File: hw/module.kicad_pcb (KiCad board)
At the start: 2 copper layers, 30 x 30 mm, 1 part

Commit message: Footprint assignment
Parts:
- added C1: 10n, Capacitor_SMD:C_0201_0603Metric_Pad0.64x0.40mm_HandSolder, F.Cu at (99.5, 62.5)
- added C10: 10n, Capacitor_SMD:C_0201_0603Metric_Pad0.64x0.40mm_HandSolder, F.Cu at (106.8, 52.8)
- added C11: 100n, Capacitor_SMD:C_0805_2012Metric_Pad1.18x1.45mm_HandSolder, F.Cu at (95.7, 63.1)
- added C12: 100n, Capacitor_SMD:C_0805_2012Metric_Pad1.18x1.45mm_HandSolder, F.Cu at (90.9, 65.9)
- added C13: 100n, Capacitor_SMD:C_0805_2012Metric_Pad1.18x1.45mm_HandSolder, F.Cu at (90.9, 62.9)
- added C14: 100n, Capacitor_SMD:C_0805_2012Metric_Pad1.18x1.45mm_HandSolder, F.Cu at (102.9, 53.4)
- added C2: 10n, Capacitor_SMD:C_0201_0603Metric_Pad0.64x0.40mm_HandSolder, F.Cu at (84.5, 67.4)
- added C3: 100n, Capacitor_SMD:C_0201_0603Metric_Pad0.64x0.40mm_HandSolder, F.Cu at (94.7, 65.5)
- added C4: 100n, Capacitor_SMD:C_0201_0603Metric_Pad0.64x0.40mm_HandSolder, F.Cu at (105.6, 58.0)
- added C5: 200p, Capacitor_SMD:C_0201_0603Metric_Pad0.64x0.40mm_HandSolder, F.Cu at (102.8, 57.6)
- added C6: 200p, Capacitor_SMD:C_0201_0603Metric_Pad0.64x0.40mm_HandSolder, F.Cu at (106.8, 54.5)
- added C7: 10n, Capacitor_SMD:C_0201_0603Metric_Pad0.64x0.40mm_HandSolder, F.Cu at (94.7, 67.3)
- added C8: 100n, Capacitor_SMD:C_0201_0603Metric_Pad0.64x0.40mm_HandSolder, F.Cu at (105.6, 56.3)
- added C9: 100n, Capacitor_SMD:C_0201_0603Metric_Pad0.64x0.40mm_HandSolder, F.Cu at (109.6, 52.8)
- added L1: L, Inductor_SMD:L_0201_0603Metric_Pad0.64x0.40mm_HandSolder, F.Cu at (108.4, 56.3)
- added R1: 10k, Resistor_SMD:R_0201_0603Metric_Pad0.64x0.40mm_HandSolder, F.Cu at (100.0, 59.2)
- added R2: 10k, Resistor_SMD:R_0201_0603Metric_Pad0.64x0.40mm_HandSolder, F.Cu at (97.5, 67.3)
- added R3: 800k, Resistor_SMD:R_0201_0603Metric_Pad0.64x0.40mm_HandSolder, F.Cu at (102.8, 55.8)
- added R4: 800k, Resistor_SMD:R_0201_0603Metric_Pad0.64x0.40mm_HandSolder, F.Cu at (97.5, 65.5)
- added R5: R, Resistor_SMD:R_0201_0603Metric_Pad0.64x0.40mm_HandSolder, F.Cu at (102.3, 61.1)
- added R6: 500k, Resistor_SMD:R_0201_0603Metric_Pad0.64x0.40mm_HandSolder, F.Cu at (109.6, 54.5)
- added R7: 500k, Resistor_SMD:R_0201_0603Metric_Pad0.64x0.40mm_HandSolder, F.Cu at (100.0, 57.5)
- added R8: 10k, Resistor_SMD:R_0201_0603Metric_Pad0.64x0.40mm_HandSolder, F.Cu at (102.8, 59.3)
- added TP1: SWDIO, TestPoint:TestPoint_Pad_3.0x3.0mm, F.Cu at (91.0, 58.9)
- added TP2: SWCLK, TestPoint:TestPoint_Pad_3.0x3.0mm, F.Cu at (96.0, 59.1)
- added U1: CFPS-39, Oscillator:Oscillator_SMD_Fox_FT5H_5.0x3.2mm, F.Cu at (85.8, 55.6)
- added U2: CFPS-39, Oscillator:Oscillator_SMD_Fox_FT5H_5.0x3.2mm, F.Cu at (85.8, 62.9)
- added U3: 74LVC1G125, Package_TO_SOT_SMD:SOT-23-5_HandSoldering, F.Cu at (124.5, 66.5)
- added U4: mux, Package_TO_SOT_SMD:SOT-363_SC-70-6_Handsoldering, F.Cu at (124.5, 62.2)
- added U5: MAX919, Package_TO_SOT_SMD:SOT-23-5_HandSoldering, F.Cu at (97.6, 54.2)
- added U6: STM32L010F4P6, farnell:STM32L010F4P6, F.Cu at (115.9, 68.4)
- added U7: BAS70-7-F, Package_TO_SOT_SMD:SOT-143_Handsoldering, F.Cu at (91.6, 54.1)

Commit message: PCB arrange
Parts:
- moved U4 76.0 mm to (49.0, 52.9), turned to -90 degrees
- moved U3 75.6 mm to (51.2, 48.0), turned to 90 degrees
- moved R6 64.2 mm to (45.4, 56.8)
- moved L1 62.5 mm to (46.6, 65.4), turned to 90 degrees
- moved U6 62.5 mm to (53.6, 63.5), turned to -90 degrees
- moved R5 56.9 mm to (46.0, 69.2)
- moved C1 56.8 mm to (44.4, 48.8), turned to -90 degrees
- moved C14 54.0 mm to (49.2, 58.2)
- moved C6 51.7 mm to (56.2, 43.6)
- moved R7 51.0 mm to (49.0, 56.8)
- moved R2 50.9 mm to (52.0, 44.4)
- moved R1 50.0 mm to (52.0, 45.2)
- moved C11 48.3 mm to (47.6, 67.6)
- moved R8 47.4 mm to (55.4, 57.8), turned to -90 degrees
- moved R4 47.1 mm to (56.2, 42.8)
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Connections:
- U7 pad 1: Net-(C6-Pad1) -> Net-(R1-Pad2)
- U7 pad 2: Net-(R1-Pad2) -> Net-(C6-Pad1)
- U7 pad 3: Net-(C5-Pad2) -> Net-(R2-Pad2)
- U7 pad 4: Net-(R2-Pad2) -> Net-(C5-Pad2)

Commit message: PCB wiring
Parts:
- moved C3 38.5 mm to (53.3, 50.8), turned to 180 degrees
- moved C7 36.8 mm to (53.3, 67.9), turned to 180 degrees
- moved C8 30.2 mm to (53.3, 69.2), turned to 180 degrees
- moved C9 25.2 mm to (61.6, 59.1), turned to 90 degrees
- moved C10 25.1 mm to (59.1, 62.2), turned to 90 degrees
- moved C4 23.1 mm to (60.3, 59.1), turned to 90 degrees
- moved C6 8.58 mm to (62.4, 49.5), turned to 90 degrees
- moved R4 6.94 mm to (61.2, 47.6)
- moved C2 6.83 mm to (57.8, 62.2), turned to 90 degrees
- moved U5 5.66 mm to (59.9, 51.4), turned to 90 degrees
- moved C5 4.22 mm to (55.9, 52.7)
- moved R7 4.19 mm to (49.5, 61.0), turned to 90 degrees
- moved R2 3.76 mm to (54.0, 47.6), turned to -90 degrees
- moved C13 3.74 mm to (47.0, 61.6)
- moved C1 3.53 mm to (45.7, 52.1)
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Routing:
- net +3.3V: track 0.00 -> 55.4 mm
- net /OSC_STAT: track 0.00 -> 19.5 mm
- net +3.3VA: track 0.00 -> 16.8 mm
- net /half_vref: track 0.00 -> 12.9 mm
- net Net-(C5-Pad2): track 0.00 -> 11.5 mm
- net Net-(C6-Pad1): track 0.00 -> 10.8 mm
- net /OSC: track 0.00 -> 9.85 mm
- net Net-(TP1-Pad1): track 0.00 -> 8.89 mm
- net Net-(U1-Pad3): track 0.00 -> 6.77 mm
- net Net-(TP2-Pad1): track 0.00 -> 6.22 mm
- net Net-(C11-Pad1): track 0.00 -> 5.46 mm
- net Net-(U2-Pad3): track 0.00 -> 5.24 mm
- net Net-(R1-Pad2): track 0.00 -> 4.85 mm
- net Net-(R8-Pad2): track 0.00 -> 3.58 mm
- net Net-(R1-Pad1): track 0.00 -> 3.29 mm
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- removed copper zone on B.Cu, net GND
- removed copper zone on F.Cu, net GND

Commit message: Pcb++
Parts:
- added C15: 1n, Capacitor_SMD:C_0201_0603Metric_Pad0.64x0.40mm_HandSolder, F.Cu at (54.6, 58.7)
- U4: value mux -> 74 LVC 1G3157GW,125
- moved C4 5.75 mm to (58.2, 64.4), turned to 0 degrees
- moved C9 5.67 mm to (58.2, 63.6), turned to 0 degrees
- moved C1 3.44 mm to (44.5, 48.9)
- moved C8 3.24 mm to (50.1, 68.6), turned to 90 degrees
- moved C7 2.49 mm to (51.0, 68.6), turned to 90 degrees
- moved C10 1.66 mm to (59.0, 60.6)
- moved C2 1.63 mm to (57.8, 60.6)
- moved C6 1.42 mm to (61.1, 49.1), turned to 0 degrees
- moved R1 0.85 mm to (54.0, 46.6)
- moved R8 0.85 mm to (51.2, 58.3)
- moved C5 0.77 mm to (56.5, 52.2), turned to 180 degrees
- moved R2 0.77 mm to (54.0, 48.4)
- moved R4 0.73 mm to (61.1, 48.4)
- moved R3 0.60 mm to (56.5, 51.4)
- moved U5 0.55 mm to (59.7, 52.0)
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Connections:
- U6 pad 14: unconnected-(U6-Pad14) -> /RX
- U6 pad 17: /RX -> /TX
- U6 pad 18: /TX -> /RX
- U6 pad 2: /OSC_STAT -> unconnected-(U6-Pad2)
- U6 pad 3: unconnected-(U6-Pad3) -> /OSC_STAT
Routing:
- net /RX: track 0.00 -> 121.6 mm, vias 8 -> 11
- net /TX: track 0.00 -> 120.6 mm
- net +3.3V: track 55.4 -> 167.4 mm, vias 8 -> 10
- net GND: track 0.00 -> 5.25 mm, vias 8 -> 53
- net Net-(U2-Pad3): track 5.24 -> 8.21 mm, vias 0 -> 2
- net /OSC_STAT: track 19.5 -> 17.5 mm
- net Net-(C6-Pad1): track 10.8 -> 9.36 mm
- net Net-(R8-Pad2): track 3.58 -> 4.82 mm
- net Net-(C5-Pad2): track 11.5 -> 10.6 mm
- net Net-(R2-Pad2): track 2.16 -> 1.31 mm
- net +3.3VA: track 16.8 -> 16.0 mm
- net (no net): vias 2 -> 0
- added copper zone on B.Cu, net GND
- added copper zone on F.Cu, net GND

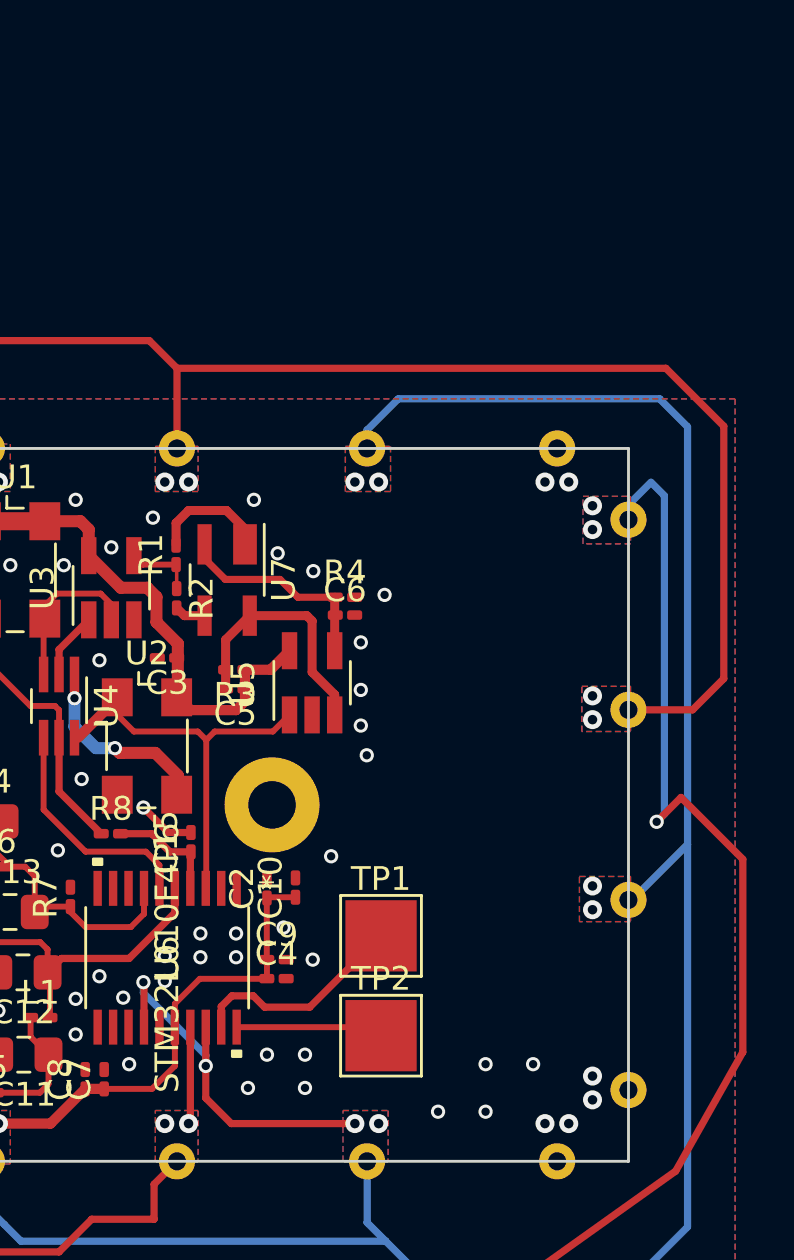
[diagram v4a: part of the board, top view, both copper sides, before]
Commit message: Add 3D models
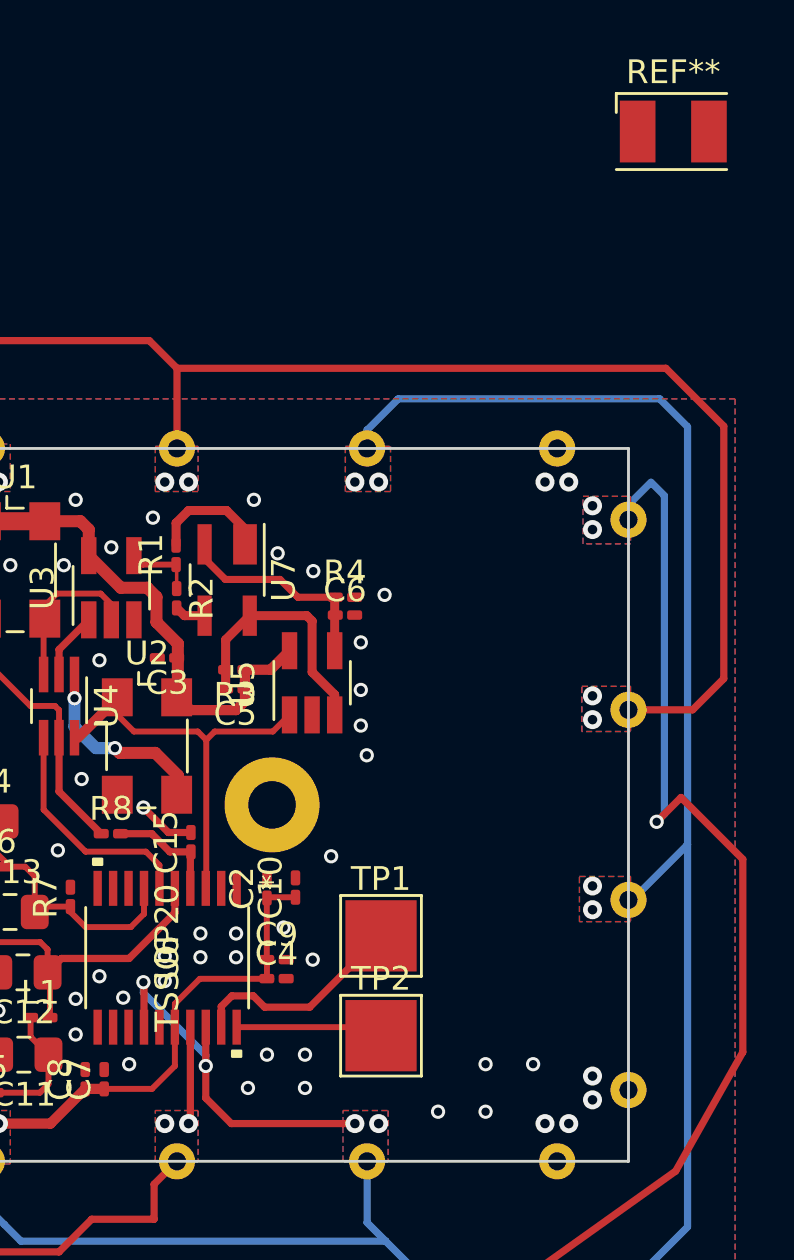
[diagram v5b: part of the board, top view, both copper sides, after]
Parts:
- added REF**: LED_PLCC-2, LED_SMD:LED_PLCC-2, F.Cu at (74.9, 28.8)
- U6: value STM32L010F4P6 -> TSSOP20

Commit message: Footprint fix, and first PCB release
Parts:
- removed REF**: LED_PLCC-2, LED_SMD:LED_PLCC-2
- added C16: 4u7, Capacitor_SMD:C_0402_1005Metric_Pad0.74x0.62mm_HandSolder, F.Cu at (69.2, 63.0)
- added C17: 4u7, Capacitor_SMD:C_0402_1005Metric_Pad0.74x0.62mm_HandSolder, F.Cu at (69.2, 64.1)
- added C18: 4u7, Capacitor_SMD:C_0402_1005Metric_Pad0.74x0.62mm_HandSolder, F.Cu at (69.2, 65.2)
- added C19: 4u7, Capacitor_SMD:C_0402_1005Metric_Pad0.74x0.62mm_HandSolder, F.Cu at (69.2, 66.3)
- added C20: 4u7, Capacitor_SMD:C_0402_1005Metric_Pad0.74x0.62mm_HandSolder, F.Cu at (69.2, 67.4)
- added C21: 4u7, Capacitor_SMD:C_0402_1005Metric_Pad0.74x0.62mm_HandSolder, F.Cu at (69.2, 68.5)
- added C22: 200p, Capacitor_SMD:C_0201_0603Metric_Pad0.64x0.40mm_HandSolder, F.Cu at (62.0, 56.8)
- added Q1: MUN 2211, Package_TO_SOT_SMD:SOT-23_Handsoldering, F.Cu at (69.0, 52.6)
- added R11: 150k, Resistor_SMD:R_0201_0603Metric_Pad0.64x0.40mm_HandSolder, F.Cu at (69.7, 59.7)
- added R12: 150k, Resistor_SMD:R_0201_0603Metric_Pad0.64x0.40mm_HandSolder, F.Cu at (69.7, 61.6)
- added R9: 100, Resistor_SMD:R_0201_0603Metric_Pad0.64x0.40mm_HandSolder, F.Cu at (66.5, 45.9)
- added U8: SS39ET, Package_TO_SOT_SMD:SOT-23_Handsoldering, F.Cu at (69.0, 47.0)
- L1: value L -> 27n
- R5: value R -> 10
- U1, U2: footprint Oscillator:Oscillator_SMD_Fox_FT5H_5.0x3.2mm -> Oscillator:Oscillator_SMD_EuroQuartz_XO32-4Pin_3.2x2.5mm_HandSoldering
- U6: value TSSOP20 -> STM32L010F4P6
- moved U1 0.73 mm to (46.7, 46.7), turned to -90 degrees
- moved U2 0.69 mm to (53.4, 55.0), turned to -90 degrees
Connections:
- U6 pad 2: unconnected-(U6-Pad2) -> /hall_on
- U6 pad 8: unconnected-(U6-Pad8) -> /hall_exp
- U6 pad 9: unconnected-(U6-Pad9) -> /Cap_experiment
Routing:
- net /Cap_experiment: track 0.00 -> 28.7 mm, vias 0 -> 2
- net /hall_exp: track 0.00 -> 28.7 mm, vias 0 -> 2
- net /hall_on: track 0.00 -> 17.0 mm, vias 0 -> 2
- net +3.3V: track 167.4 -> 183.6 mm, vias 10 -> 11
- net Net-(Q1-Pad3): track 0.00 -> 2.60 mm
- net GND: track 5.25 -> 7.59 mm, vias 53 -> 61
- net Net-(U1-Pad3): track 6.77 -> 8.77 mm
- net Net-(R9-Pad1): track 0.00 -> 1.50 mm
- net /half_vref: track 12.9 -> 14.4 mm
- net Net-(R11-Pad2): track 0.00 -> 1.07 mm
- net /OSC_STAT: track 17.5 -> 17.6 mm, vias 0 -> 2

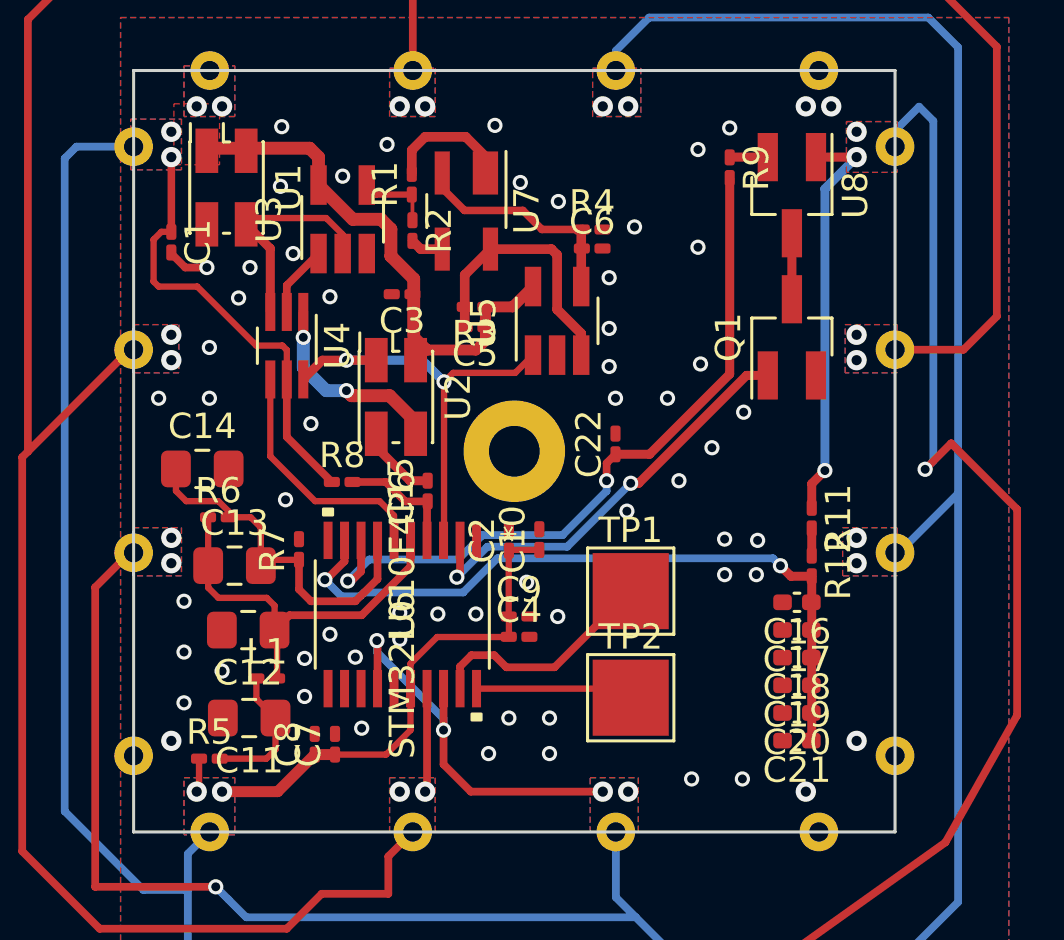
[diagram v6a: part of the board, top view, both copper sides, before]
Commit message: Final 3D models, final capacitor sizes, final capacitor numbers, final capacitor placements
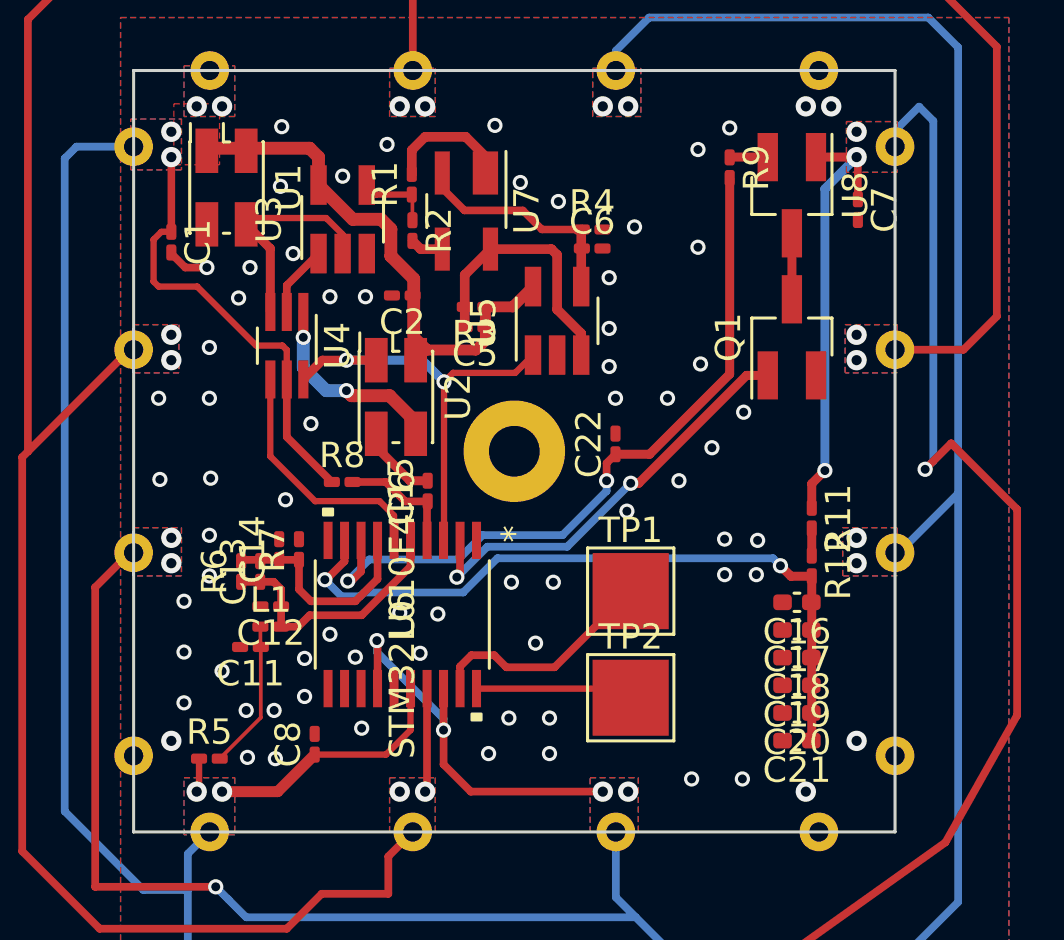
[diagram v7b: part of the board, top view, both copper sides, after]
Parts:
- removed C10: 10n, Capacitor_SMD:C_0201_0603Metric_Pad0.64x0.40mm_HandSolder
- removed C3, C4, C9: 100n, Capacitor_SMD:C_0201_0603Metric_Pad0.64x0.40mm_HandSolder
- C11, C12, C13, C14: footprint Capacitor_SMD:C_0805_2012Metric_Pad1.18x1.45mm_HandSolder -> Capacitor_SMD:C_0201_0603Metric_Pad0.64x0.40mm_HandSolder
- U1, U2: footprint Oscillator:Oscillator_SMD_EuroQuartz_XO32-4Pin_3.2x2.5mm_HandSoldering -> farnell:Oscillator_SMD_EuroQuartz_XO32-4Pin_3.2x2.5mm_HandSoldering
- moved C7 29.5 mm to (71.5, 47.6), turned to -90 degrees
- moved C2 10.5 mm to (53.6, 51.0), turned to 180 degrees
- moved C14 4.39 mm to (48.8, 61.0), turned to 90 degrees
- moved C11 2.80 mm to (47.6, 64.8)
- moved R6 2.32 mm to (47.2, 61.8), turned to 90 degrees
- moved L1 2.05 mm to (48.4, 64.0)
- moved C12 1.29 mm to (48.4, 63.2)
- moved C13 1.04 mm to (48.0, 61.8), turned to 90 degrees
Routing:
- net +3.3V: track 183.6 -> 175.2 mm
- net /half_vref: track 14.4 -> 8.64 mm
- net +3.3VA: track 16.0 -> 10.3 mm
- net GND: vias 61 -> 70
